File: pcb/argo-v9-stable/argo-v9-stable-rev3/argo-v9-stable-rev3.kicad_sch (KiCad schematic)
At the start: 102 parts, among them IC1 MP2672GD, J1 Sparkfun_NEO-N9M-SMA, J2 USB4125-GF-A, J3 LED_power_button_RGB_LED, J4 Conn_I2C_Molex_705450003, J5 Conn_I2C_Molex_705450003, K1 PRL3-5V-DC-1A, Q1 BSD840N, Q2 BSD840N, SW1 POW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

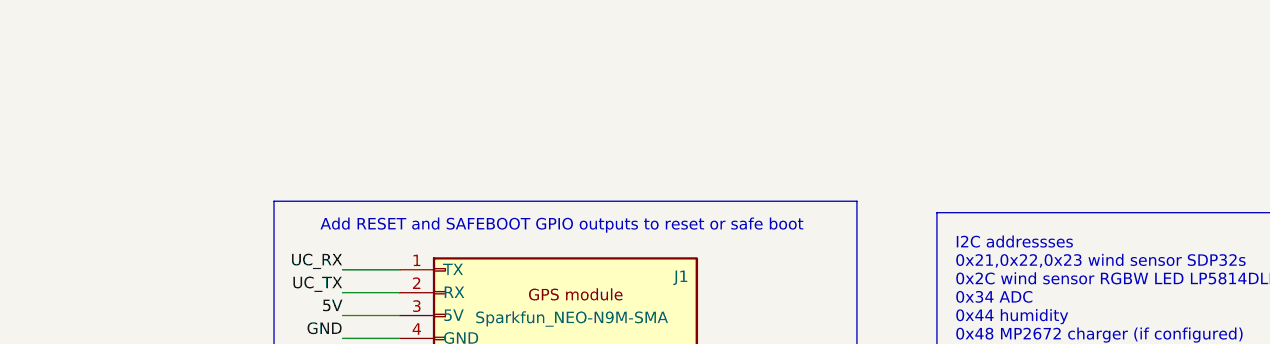
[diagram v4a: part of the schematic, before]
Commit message: added notes about I2C, adding optional pullups to 5V I2C for long wind seensor cable.
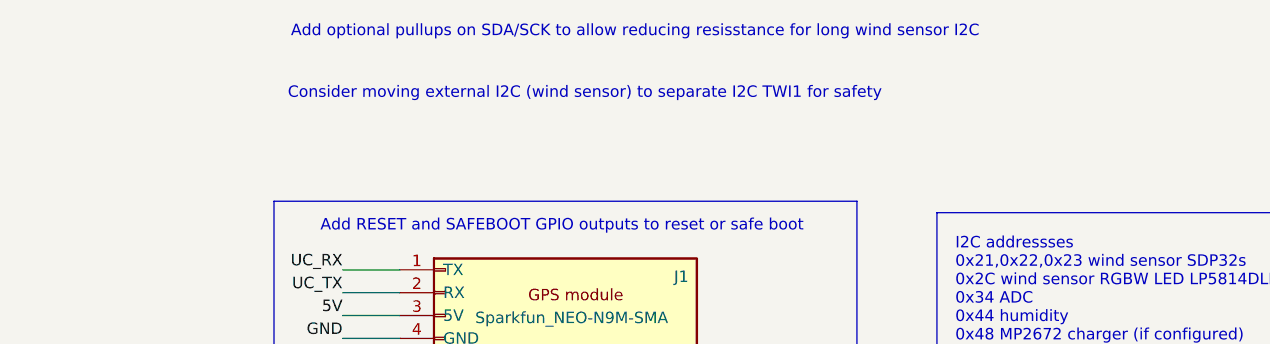
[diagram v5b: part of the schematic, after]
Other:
- note added: "Add optional pullups on SDA/SCK to allow reducing resisstance for long wind sensor I2C"
- note added: "Consider moving external I2C (wind sensor) to separate I2C TWI1 for safety"
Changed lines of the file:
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@@
 				(thickness 0.254)
 				(bold yes)
-				(color 255 0 255 1)
+				(color 0 132 0 1)
 			)
 			(justify top)
@@
 		)
 	)
+	(text "Consider moving external I2C (wind sensor) to separate I2C TWI1 for safety"
+		(exclude_from_sim no)
+		(at 203.454 37.592 0)
+		(effects
+			(font
+				(size 1.27 1.27)
+				(color 255 0 0 1)
+			)
+		)
+	)
 	(text "Fully charged battery makes 8.4V.\nRtop=27k Rbot=18k, then vout=0.4vin, \nso 8.4V will give 3.36V"
 		(exclude_from_sim no)
@@
 			(font
 				(size 0.889 0.889)
-				(color 255 0 255 1)
+				(color 0 132 0 1)
 			)
 		)
@@
 			(font
 				(size 0.9 0.9)
+				(color 0 132 0 1)
+			)
+			(justify left)
+		)
+	)
+	(text "ADC for battery voltage, \nsaltwater, and sail winch current"
+		(exclude_from_sim no)
+		(at 88.392 203.2 0)
+		(effects
+			(font
+				(size 1.27 1.27)
+			)
+		)
+	)
+	(text "Add optional pullups on SDA/SCK to allow reducing resisstance for long wind sensor I2C"
+		(exclude_from_sim no)
+		(at 209.042 30.734 0)
+		(effects
+			(font
+				(size 1.27 1.27)
+				(color 255 0 0 1)
+			)
+		)
+	)
+	(text "Solder R24 to let\nOPi drive BLUE\npower button LED"
+		(exclude_from_sim no)
+		(at 176.53 112.014 0)
+		(effects
+			(font
+				(size 0.889 0.889)
+				(color 0 132 0 1)
+			)
+			(justify left)
+		)
+	)
+	(text "POW_OFF=1 \ndisconnects \nlatching\npower relay"
+		(exclude_from_sim no)
+		(at 176.784 141.224 0)
+		(effects
+			(font
+				(size 1.016 1.016)
+			)
+			(justify left)
+		)
+	)
+	(text "Humidity sensor"
+		(exclude_from_sim no)
+		(at 231.648 127 0)
+		(effects
+			(font
+				(size 1.27 1.27)
+			)
+		)
+	)
+	(text "R12: standalone\nsolder for standalone"
+		(exclude_from_sim no)
+		(at 335.28 96.774 0)
+		(effects
+			(font
+				(size 1.016 1.016)
 				(color 255 0 255 1)
 			)
-			(justify left)
-		)
-	)
-	(text "ADC for battery voltage, \nsaltwater, and sail winch current"
-		(exclude_from_sim no)
-		(at 88.392 203.2 0)
-		(effects
-			(font
-				(size 1.27 1.27)
-			)
-		)
-	)
-	(text "Solder R24 to let\nOPi drive BLUE\npower button LED"
-		(exclude_from_sim no)
-		(at 176.53 112.014 0)
-		(effects
-			(font
-				(size 0.889 0.889)
-				(color 255 0 255 1)
-			)
-			(justify left)
-		)
-	)
-	(text "POW_OFF=1 \ndisconnects \nlatching\npower relay"
-		(exclude_from_sim no)
-		(at 176.784 141.224 0)
-		(effects
-			(font
-				(size 1.016 1.016)
-			)
-			(justify left)
-		)
-	)
-	(text "Humidity sensor"
-		(exclude_from_sim no)
-		(at 231.648 127 0)
-		(effects
-			(font
-				(size 1.27 1.27)
-			)
-		)
-	)
-	(text "R12: standalone\nsolder for standalone"
-		(exclude_from_sim no)
-		(at 335.28 96.774 0)
-		(effects
-			(font
-				(size 1.016 1.016)
-				(color 255 0 255 1)
-			)
 		)
 	)
@@
 			(font
 				(size 1.1176 1.1176)
-				(color 255 0 255 1)
+				(color 0 132 0 1)
 			)
 			(justify left)
@@
 			(font
 				(size 0.889 0.889)
-				(color 255 0 255 1)
-			)
-			(justify left)
+				(color 0 132 0 1)
+			)
+			(justify left)

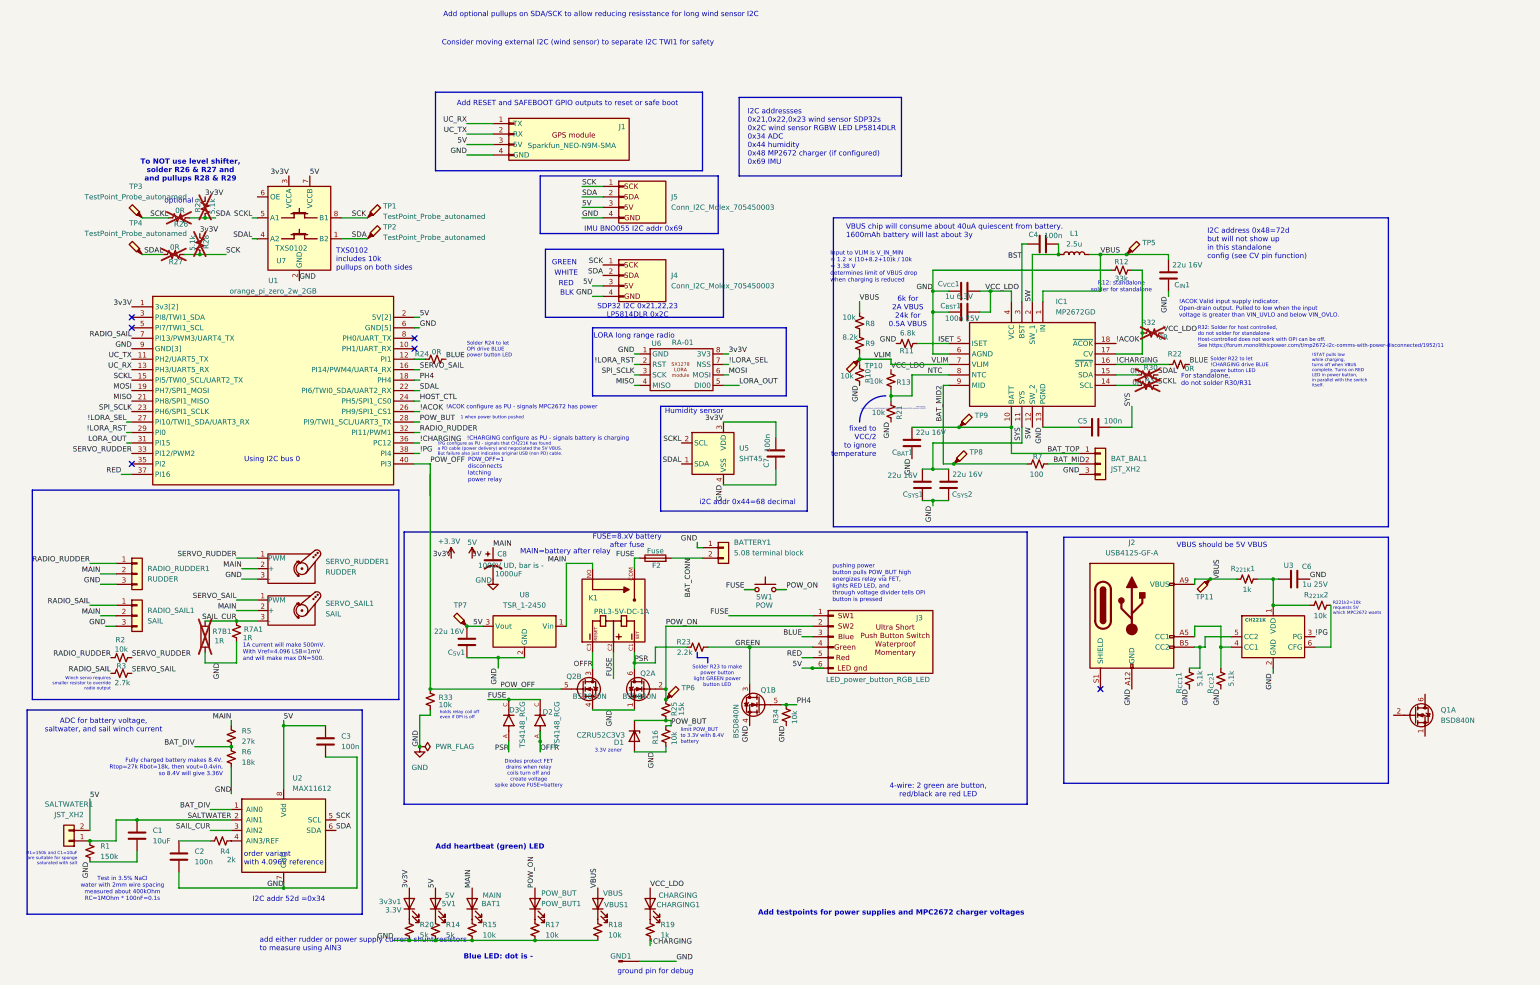
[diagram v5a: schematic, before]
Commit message: rev4 argo pcb and rev1c windsensor pcb - fixed critical incorrect connection on rev3 pcb that was destroying the gate of the power relay NFET by overvoltage - fixed critical missing connection tying OE high for I2C level converter - fixed critical I2C address conflict on 0x34 by replacing LED controller on windsensor - replaced RGBW LED with one that is hand solderable on wind sensor - added buzzer to argo PCB to signal SOS startup and shutddown events - many cosmetic impprrovements - added power off button to allow forcing relay off in case of stuck software - 3d model of wind sensor matches PCB and verified mechaniically correct. - Other parts (cable gland and mast step up) are verified correct.
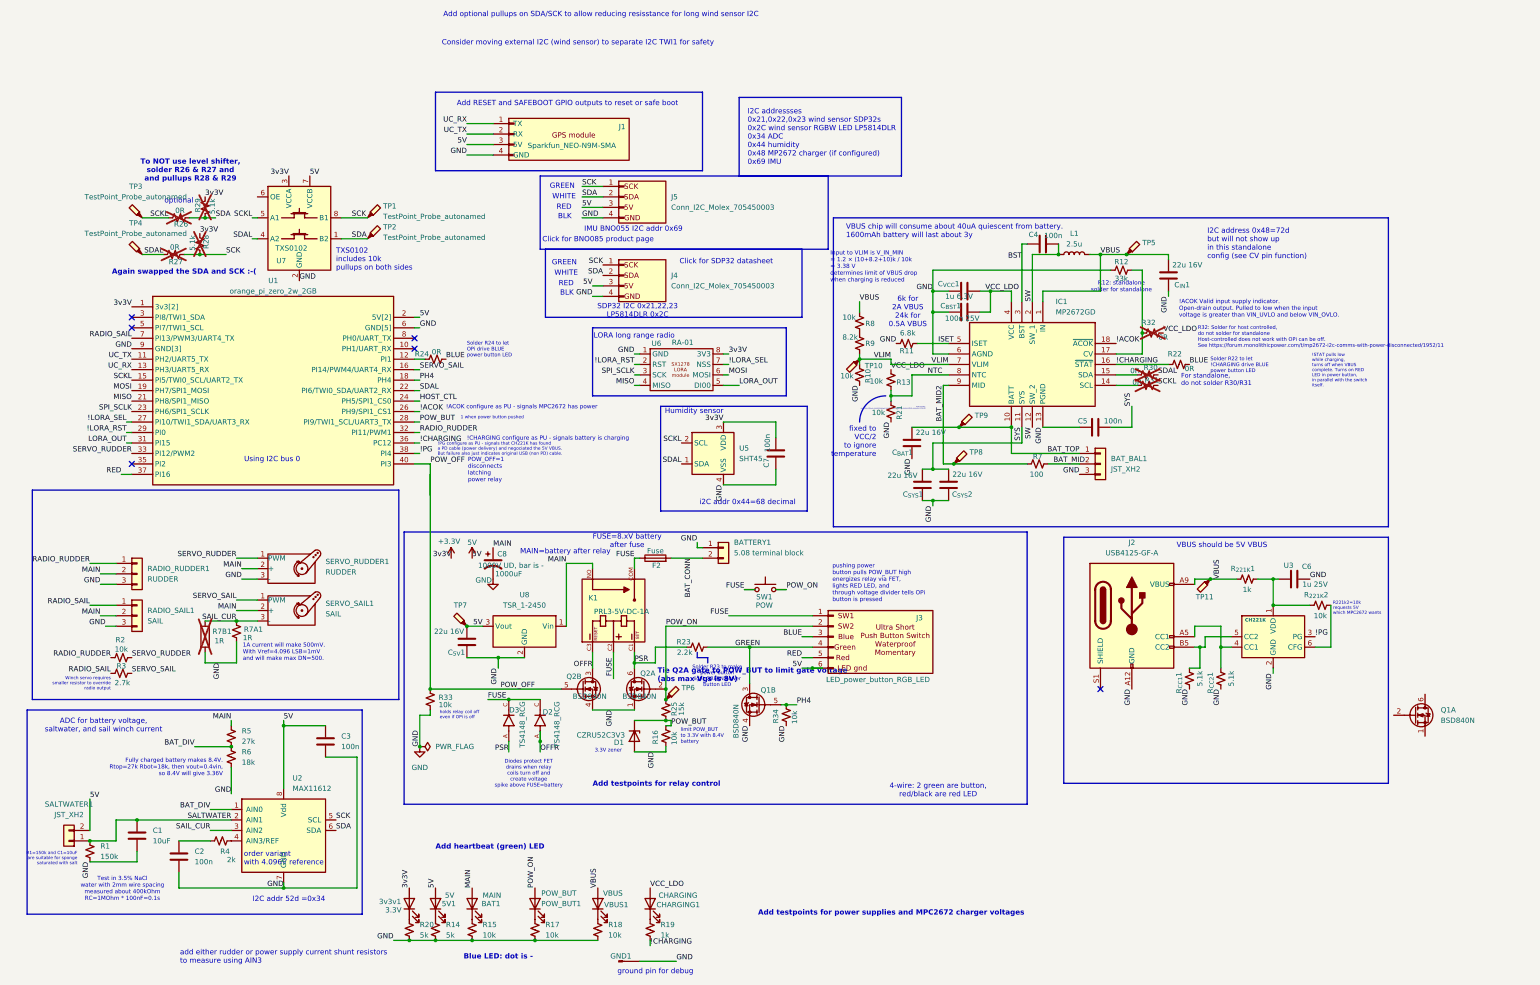
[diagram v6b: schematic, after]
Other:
- note added: "Add testpoints for relay control"
- note added: "Again swapped the SDA and SCK :-("
- note added: "Click for BNO085 product page"
- note added: "Click for SDP32 datasheet"
- note added: "Tie Q2A gate to POW_BUT to limit gate voltage (abs max Vgs is 8V)"
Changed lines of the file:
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@@
 	(rectangle
 		(start 194.31 69.85)
-		(end 237.49 83.82)
+		(end 264.16 87.63)
 		(stroke
 			(width 0)
@@
 	(rectangle
 		(start 195.58 87.63)
-		(end 238.76 104.14)
+		(end 257.81 104.14)
 		(stroke
 			(width 0)
@@
 		)
 	)
+	(text "Click for SDP32 datasheet\n"
+		(exclude_from_sim no)
+		(at 228.092 90.678 0)
+		(effects
+			(font
+				(size 1.27 1.27)
+				(color 0 0 255 1)
+			)
+			(justify left)
+			(href "https://sensirion.com/products/catalog/SDP32")
+		)
+	)
 	(text "Add testpoints for power supplies and MPC2672 charger voltages"
 		(exclude_from_sim no)
@@
 	(text "add either rudder or power supply current shunt resistors\nto measure using AIN3"
 		(exclude_from_sim no)
-		(at 126.238 256.286 0)
+		(at 106.934 259.334 0)
 		(effects
 			(font
@@
 		)
 	)
+	(text "Add testpoints for relay control"
+		(exclude_from_sim no)
+		(at 207.01 217.424 0)
+		(effects
+			(font
+				(size 1.27 1.27)
+				(thickness 0.254)
+				(bold yes)
+				(color 255 0 0 1)
+			)
+			(justify left)
+		)
+	)
 	(text "Fully charged battery makes 8.4V.\nRtop=27k Rbot=18k, then vout=0.4vin, \nso 8.4V will give 3.36V"
 		(exclude_from_sim no)
@@
 			(font
 				(size 1 1)
+				(color 0 0 0 1)
+			)
+			(justify right)
+		)
+	)
+	(text "BLK"
+		(exclude_from_sim no)
+		(at 201.93 79.756 0)
+		(effects
+			(font
+				(size 1.27 1.27)
 				(color 0 0 0 1)
 			)
@@
 		)
 	)
+	(text "Click for BNO085 product page\n"
+		(exclude_from_sim no)
+		(at 194.818 85.344 0)
+		(effects
+			(font
+				(size 1.27 1.27)
+				(color 0 0 255 1)
+			)
+			(justify left)
+			(href "https://www.adafruit.com/product/4754?srsltid=AfmBOoqq5LXPUfSRLzIPW6EC369kqhWas1ZF4KPSplO_62JEXQH6ESZj")
+		)
+	)
 	(text "Winch servo requires\nsmaller resistor to override\nradio output"
 		(exclude_from_sim no)
@@
 		)
 	)
+	(text "Again swapped the SDA and SCK :-("
+		(exclude_from_sim no)
+		(at 107.95 93.218 0)
+		(effects
+			(font
+				(size 1.27 1.27)
+				(thickness 0.254)
+				(bold yes)
+				(color 255 0 0 1)
+			)
+		)
+	)
 	(text "!CHARGING configure as PU - signals battery is charging"
 		(exclude_from_sim no)
@@
 		)
 	)
+	(text "Tie Q2A gate to POW_BUT to limit gate voltage\n(abs max Vgs is 8V)"
+		(exclude_from_sim no)
+		(at 222.758 191.008 0)
+		(effects
+			(font
+				(size 1.27 1.27)
+				(thickness 0.254)
+				(bold yes)
+				(color 255 0 0 1)
+			)
+			(justify left)
+		)
+	)
 	(text "Solder R24 to let\nOPi drive BLUE\npower button LED"
 		(exclude_from_sim no)
@@
 		)
 	)
+	(text "GREEN"
+		(exclude_from_sim no)
+		(at 202.692 72.39 0)
+		(effects
+			(font
+				(size 1.27 1.27)
+				(color 0 255 0 1)
+			)
+			(justify right)
+		)
+	)
 	(text "R12: standalone\nsolder for standalone"
 		(exclude_from_sim no)
@@
 			)
 			(justify left)
+		)
+	)
+	(text "WHITE"
+		(exclude_from_sim no)
+		(at 202.946 74.93 0)
+		(effects
+			(font
+				(size 1.27 1.27)
+				(color 194 194 194 1)
+			)
+			(justify right)
 		)
 	)
@@
 		)
 	)
+	(text "RED"
+		(exclude_from_sim no)
+		(at 201.93 77.47 0)
+		(effects
+			(font
+				(size 1.27 1.27)
+				(color 255 0 0 1)
+			)
+			(justify right)
+		)
+	)
